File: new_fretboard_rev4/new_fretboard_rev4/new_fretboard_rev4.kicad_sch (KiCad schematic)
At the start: 48 parts, among them J1 Conn_01x06, J2 Conn_01x06, U1 LX3302AQPW_TSSOP-14, U2 LX3302AQPW_TSSOP-14

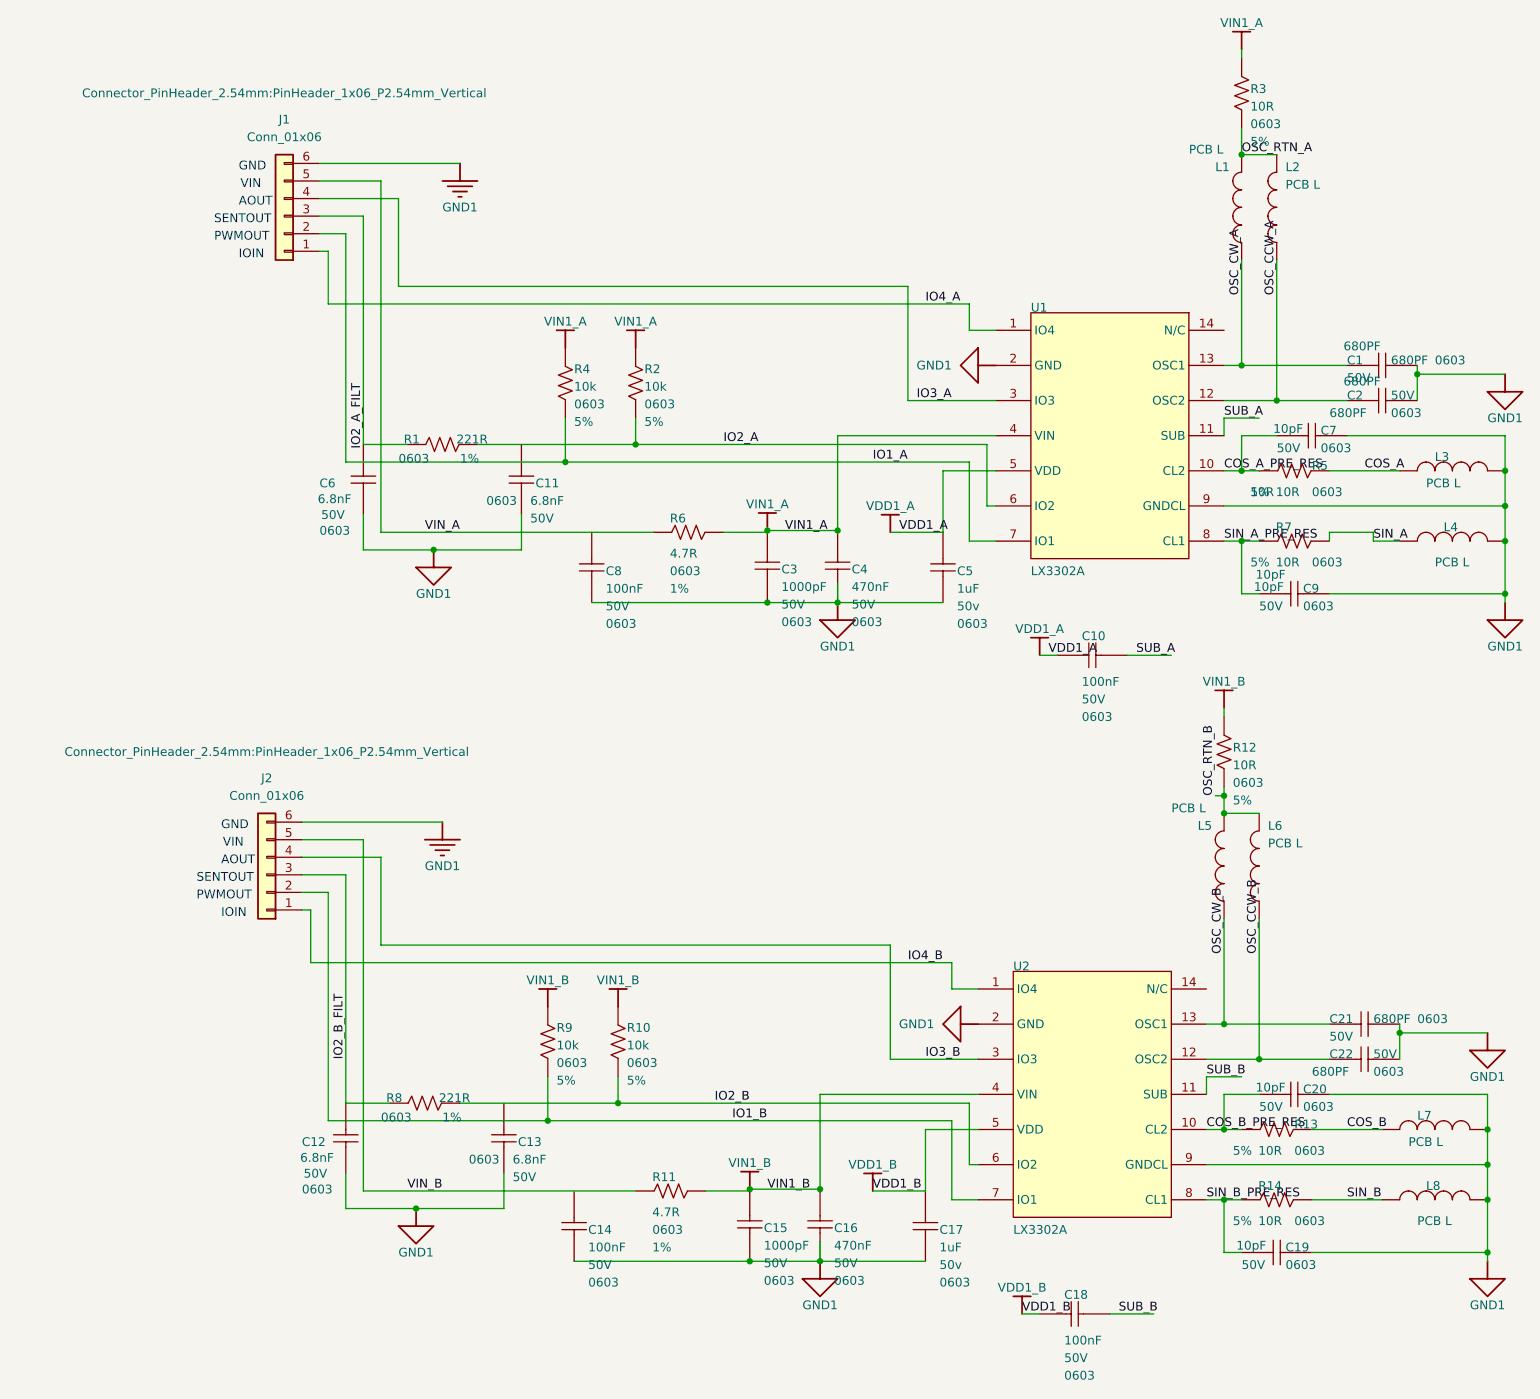
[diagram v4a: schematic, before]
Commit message: in good shape, all routed, no errors. Still single sensor strip, about to add other channels
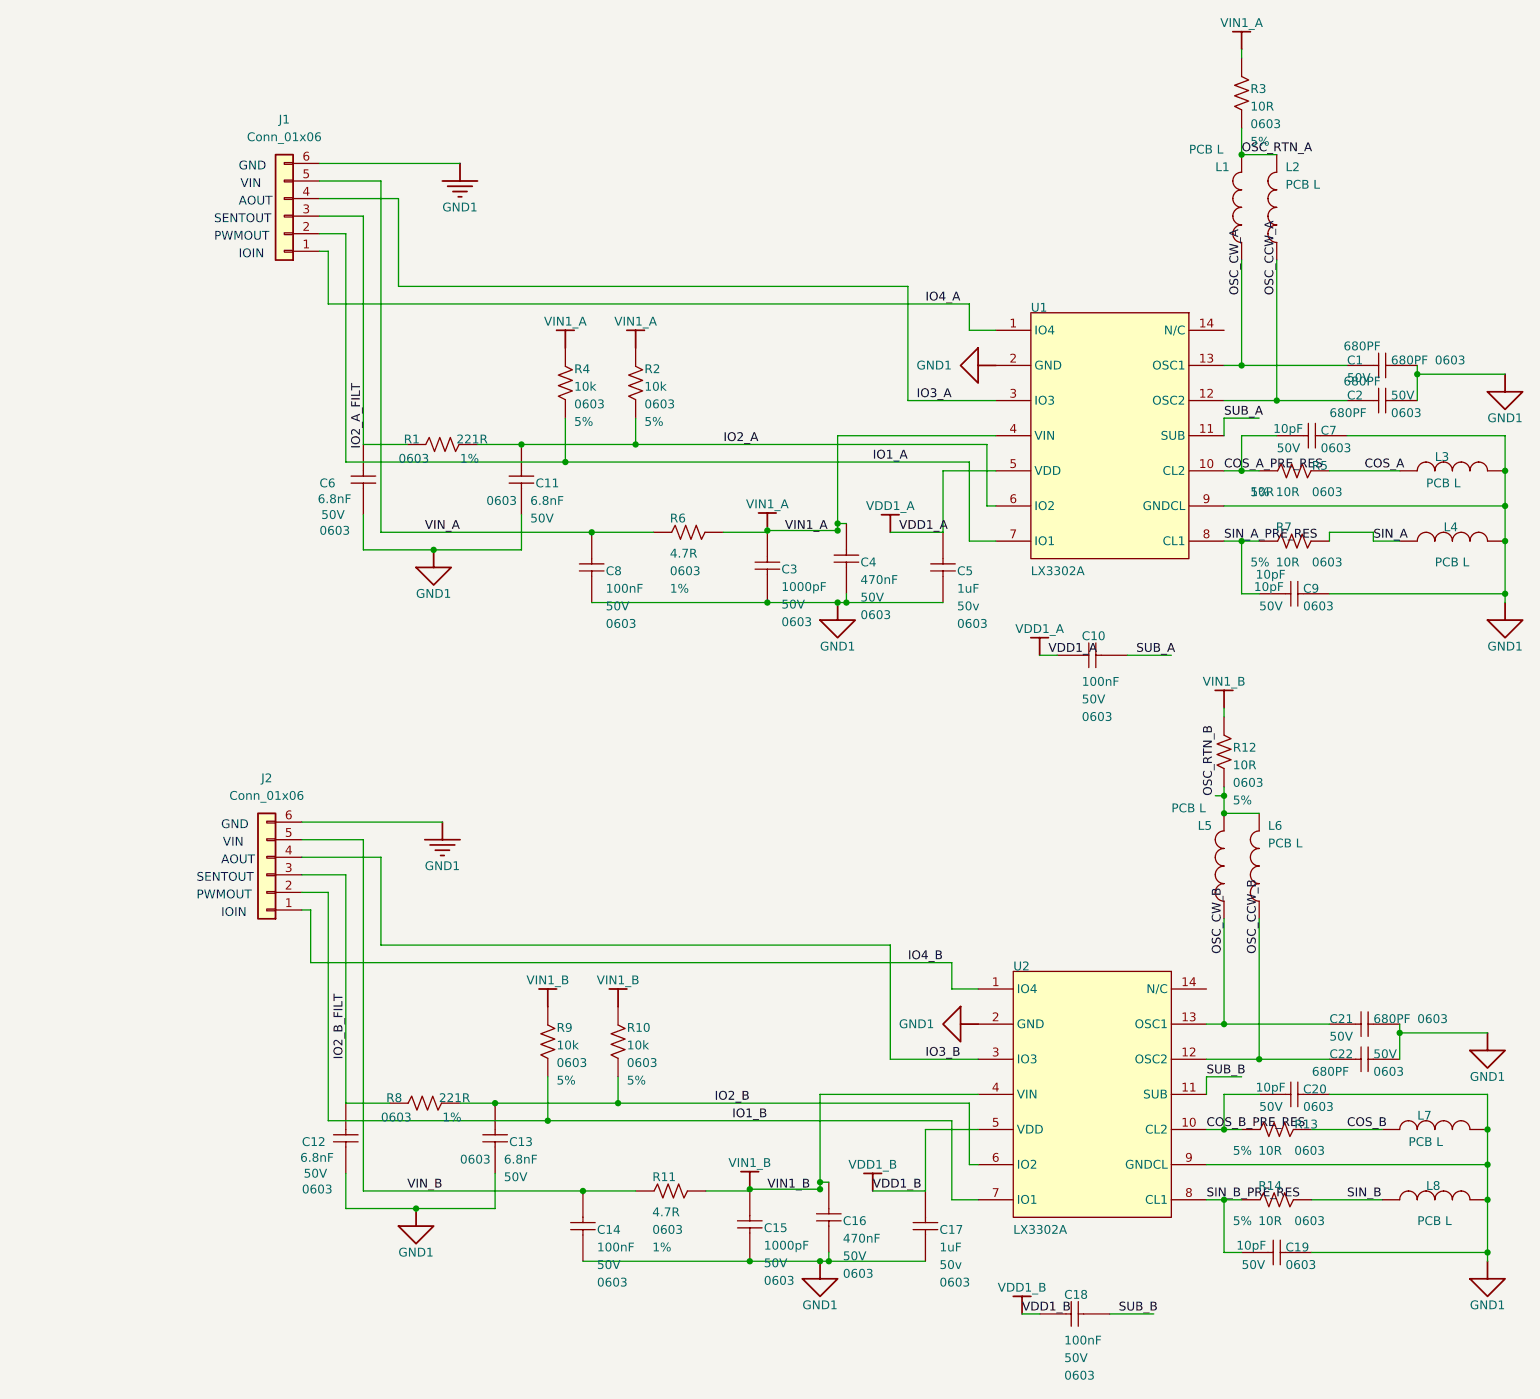
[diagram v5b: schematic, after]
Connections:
- net GND1: now also C16.1, C4.1
- net IO2_A: now also C11.2
- net IO2_B: now also C13.2
- net VIN_A: now also C8.2
- net VIN_B: now also C14.2
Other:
- moved on the sheet: C13, C14, C16, C4

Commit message: trying multichannel, reannotating
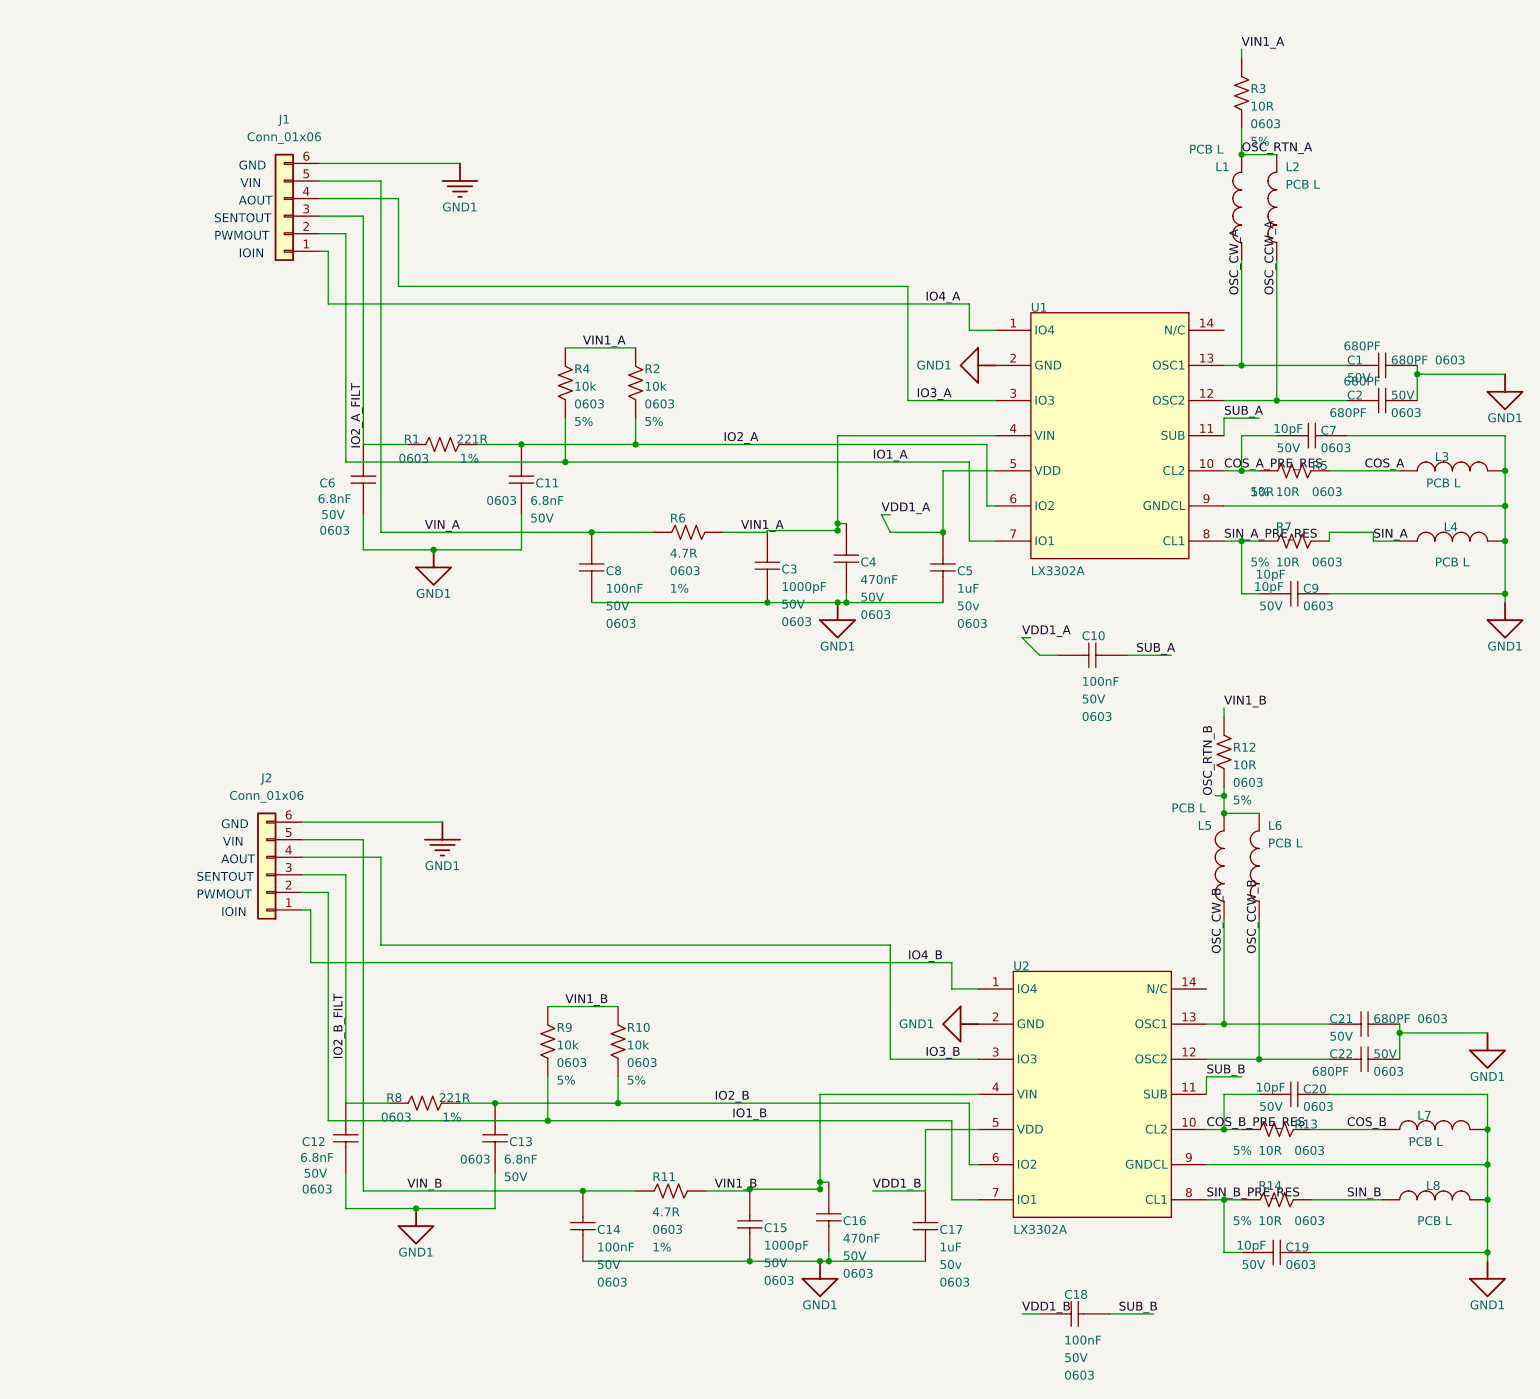
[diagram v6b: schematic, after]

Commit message: two channels done
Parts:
- J1: renamed from J2; footprint Connector_PinHeader_2.54mm:PinHeader_1x06_P2.54mm_Vertical -> Connector_PinHeader_2.54mm:PinHeader_1x05_P2.54mm_Vertical; symbol PCM_4ms_Connector:Conn_01x06 -> Connector:Conn_01x05_Pin; Specifications HEADER 1x6 MALE PINS 0.100” 180deg -> HEADER 1x5 MALE PINS 0.100” 180deg
- J2: renamed from J1; value Conn_01x06 -> Conn_01x05; footprint Connector_PinHeader_2.54mm:PinHeader_1x06_P2.54mm_Vertical -> Connector_PinHeader_2.54mm:PinHeader_1x05_P2.54mm_Vertical; symbol PCM_4ms_Connector:Conn_01x06 -> Connector:Conn_01x05_Pin; Specifications HEADER 1x6 MALE PINS 0.100” 180deg -> HEADER 1x5 MALE PINS 0.100” 180deg
- renumbered C12 to C1, C4 to C10, C17 to C11, C5 to C12, C18 to C13, C10 to C14, C19 to C15, C9 to C16, C20 to C17, C7 to C18, C21 to C19, C6 to C2, C22 to C20, C1 to C21, C2 to C22, C13 to C3, C11 to C4, C14 to C5, C8 to C6, C15 to C7, C3 to C8, C16 to C9, L5 to L1, L1 to L2, L6 to L3, L2 to L4, L7 to L5, L8 to L6, L3 to L7, L4 to L8, R8 to R1, R3 to R10, R13 to R11, R14 to R12, R5 to R13, R7 to R14, R1 to R2, R9 to R3, R10 to R5, R2 to R6, R11 to R7, R6 to R8, R12 to R9, U2 to U1, U1 to U2
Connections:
- net GND1: now also J1.1 (Pin_1), J2.1 (Pin_1); no longer J1.6 (Pin_6), J2.6 (Pin_6)
- net IO1_A: now also J2.5 (Pin_5); no longer J2.2 (Pin_2)
- net IO1_B: now also J1.5 (Pin_5); no longer J1.2 (Pin_2)
- net IO2_A_FILT: now also J2.4 (Pin_4); no longer J2.3 (Pin_3)
- net IO2_B_FILT: now also J1.4 (Pin_4); no longer J1.3 (Pin_3)
- net IO3_A: now also J2.3 (Pin_3); no longer J2.4 (Pin_4)
- net IO3_B: now also J1.3 (Pin_3); no longer J1.4 (Pin_4)
- net VIN_A: now also J2.2 (Pin_2); no longer J2.5 (Pin_5)
- net VIN_B: now also J1.2 (Pin_2); no longer J1.5 (Pin_5)
- net IO4_A: no longer names the net of U2.1 (IO4)
- net IO4_A: no longer J2.1 (Pin_1)
- net IO4_B: no longer names the net of U1.1 (IO4)
- net IO4_B: no longer J1.1 (Pin_1)
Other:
- note removed: "IOIN"
